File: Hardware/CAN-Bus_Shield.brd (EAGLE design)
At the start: 53.3 x 59.7 mm, 38 parts, among them Q1 16MHz, U1 USD-SOCKETNEW, U2 ARDUINO_SHIELDLABEL, U3 EM406, U4 MCP2515, U5 MCP2551, U6 HEX_CONVERTER, U7 JOYSTICK_MINI4UCON, X1 DB9 Plug

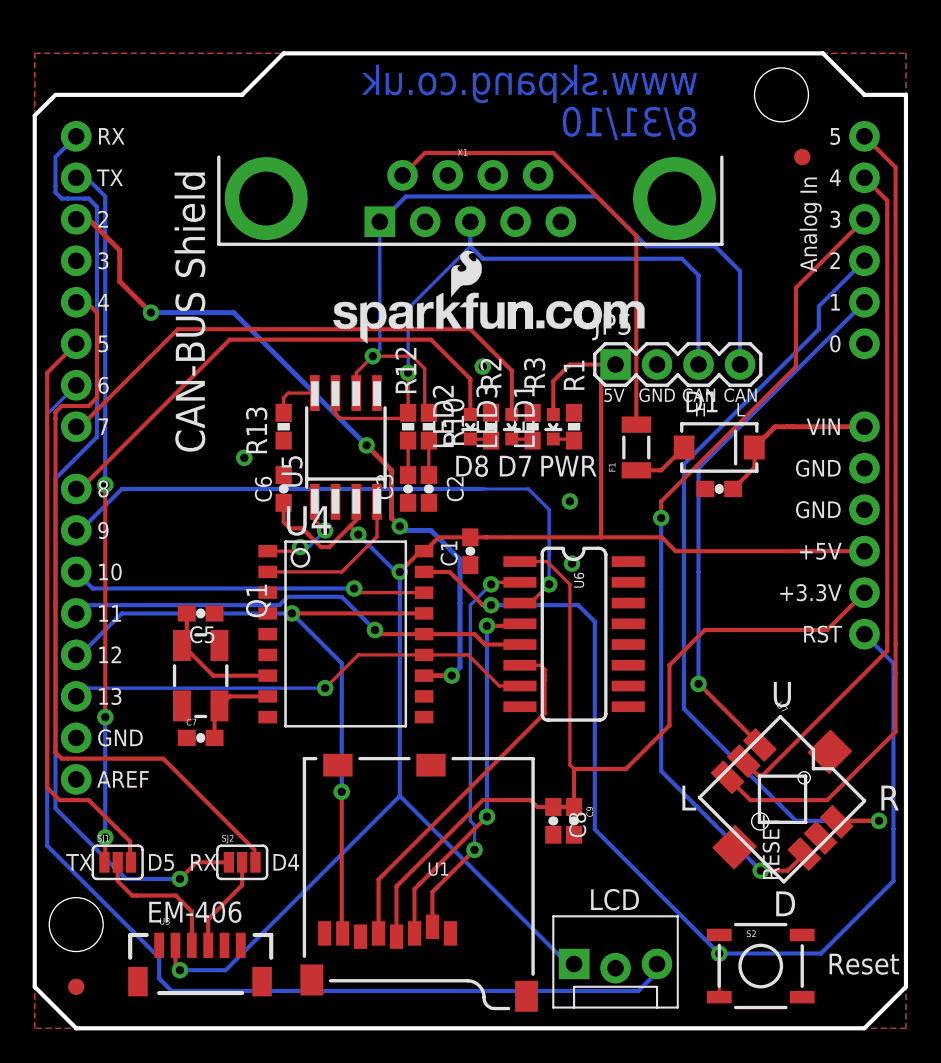
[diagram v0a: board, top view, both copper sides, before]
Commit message: Updating Board files to R3/Leonardo layout
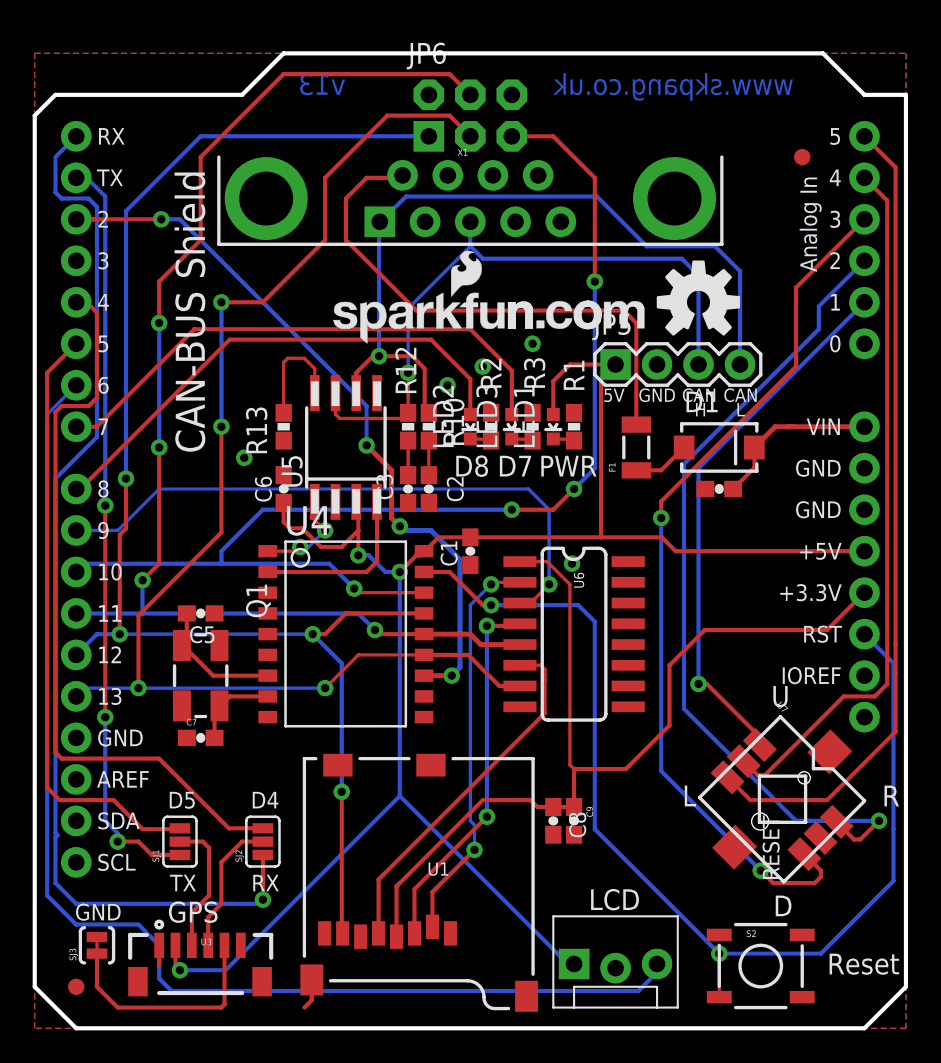
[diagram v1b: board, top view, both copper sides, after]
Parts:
- added FRAME1: FRAME-LETTER, SparkFun-Aesthetics:CREATIVE_COMMONS
- added JP6: (no value), SparkFun-Connectors:2X3-NS
- added LOGO1: OSHW-LOGOM, SparkFun-Aesthetics:OSHW-LOGO-M
- added SJ3: SOLDERJUMPERTRACE, SparkFun-Passives:SJ_2S-TRACE
- U$1: value CREATIVE_COMMONS -> REVISION; device SparkFun:CREATIVE_COMMONS -> SparkFun-Aesthetics:REVISION
- U2: value ARDUINO_SHIELDLABEL -> ARDUINO_R3_SHIELD; device SparkFun:DUEMILANOVE_SHIELD -> SparkFun-Boards:UNO_R3_SHIELD
- U3: value EM406 -> JST_VERTICAL; device SparkFun:EM406 -> SparkFun-Connectors:JST-6-SMD-VERT-1.0MM
- moved U$1 23.3 mm to (3.81, -27.9)
- moved SJ1 4.02 mm to (8.89, 11.4), turned to 90 degrees
- moved U3 2.84 mm to (10.2, 3.81)
- moved SJ2 1.80 mm to (14.0, 11.4), turned to 90 degrees
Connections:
- new net N$1: SJ3.1, U3.5
- net CAN_CS: now also JP6.5
- net GND: now also JP6.6, SJ3.2, U1.GND3; no longer U3.5
- net MISO: now also JP6.1
- net MOSI: now also JP6.4
- net SCK: now also JP6.3
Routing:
- net CAN_CS: track 21.8 -> 71.9 mm, vias 1 -> 4
- net SCK: track 28.9 -> 77.5 mm, vias 1 -> 4
- net MOSI: track 28.7 -> 76.5 mm, vias 1 -> 4
- net MISO: track 43.1 -> 87.9 mm, vias 2 -> 4
- net N$1: track 0.00 -> 14.1 mm
- net RX: track 57.6 -> 65.5 mm
- net N$13: track 28.5 -> 32.7 mm
- net N$14: track 2.95 -> 6.86 mm
- net TX: track 43.0 -> 46.2 mm
- net GND: track 0.00 -> 3.15 mm, vias 4 -> 5
- net JOY-DOWN: track 50.6 -> 53.5 mm
- net N$22: track 5.94 -> 8.48 mm
- net LCD: track 71.7 -> 73.9 mm
- net CAN_RXD: track 9.72 -> 11.6 mm
- net D5: track 35.6 -> 37.1 mm
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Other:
- board text added: "GPS"
- board text added: "T. Klopfenstein"
- board text added: "v13"
- board text removed: "8/31/10"
- board text removed: "EM-406"

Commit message: Fixing traces
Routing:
- net GND: track 3.15 -> 1.27 mm
